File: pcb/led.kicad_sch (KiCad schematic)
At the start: 45 parts, among them Q10 2N7002KDW, Q6 2N7002KDW, Q7 2N7002KDW, Q8 2N7002KDW, Q9 2N7002KDW

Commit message: Fix JLC part association
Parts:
- D10, D11, D14, D15, D16, D7, D8, D9: JLC (none) -> C72043
- D12, D13: JLC (none) -> C72041
- Q10, Q6, Q7, Q8, Q9: JLC (none) -> C2912545
- R17, R19, R23, R24, R27, R33, R36, R40, R41, R44: JLC (none) -> C25744
- R18, R20, R25, R26, R30, R32, R34, R35, R37, R39, R42, R45: JLC (none) -> C11702
- R21, R22, R28, R29, R31, R38, R43, R46: JLC (none) -> C25890

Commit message: Update blue LEDs to stocked part
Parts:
- D12, D13: JLC C72041 -> C2288
- R32, R37: value 1k -> 2k2; JLC C11702 -> C25879
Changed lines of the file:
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@@
 			)
 		)
-		(property "Datasheet" "https://datasheet.lcsc.com/lcsc/1811101510_Everlight-Elec-19-217-BHC-ZL1M2RY-3T_C72041.pdf"
+		(property "Datasheet" "https://wmsc.lcsc.com/wmsc/upload/file/pdf/v2/lcsc/1810220913_Hubei-KENTO-Elec-KT-0603B_C2288.pdf"
 			(at 152.4 121.92 0)
 			(effects
@@
 			)
 		)
-		(property "JLC" "C72041"
+		(property "JLC" "C2288"
 			(at 152.4 121.92 0)
 			(effects
@@
 			)
 		)
-		(property "Value" "1k"
+		(property "Value" "2k2"
 			(at 154.94 132.7149 0)
 			(effects
@@
 			)
 		)
-		(property "JLC" "C11702"
+		(property "JLC" "C25879"
 			(at 152.4 131.445 0)
 			(effects
@@
 			)
 		)
-		(property "Value" "1k"
+		(property "Value" "2k2"
 			(at 186.69 88.2649 0)
 			(effects
@@
 			)
 		)
-		(property "JLC" "C11702"
+		(property "JLC" "C25879"
 			(at 184.15 86.995 0)
 			(effects
@@
 			)
 		)
-		(property "Datasheet" "https://datasheet.lcsc.com/lcsc/1811101510_Everlight-Elec-19-217-BHC-ZL1M2RY-3T_C72041.pdf"
+		(property "Datasheet" "https://wmsc.lcsc.com/wmsc/upload/file/pdf/v2/lcsc/1810220913_Hubei-KENTO-Elec-KT-0603B_C2288.pdf"
 			(at 184.15 77.47 0)
 			(effects
@@
 			)
 		)
-		(property "JLC" "C72041"
+		(property "JLC" "C2288"
 			(at 184.15 77.47 0)
 			(effects

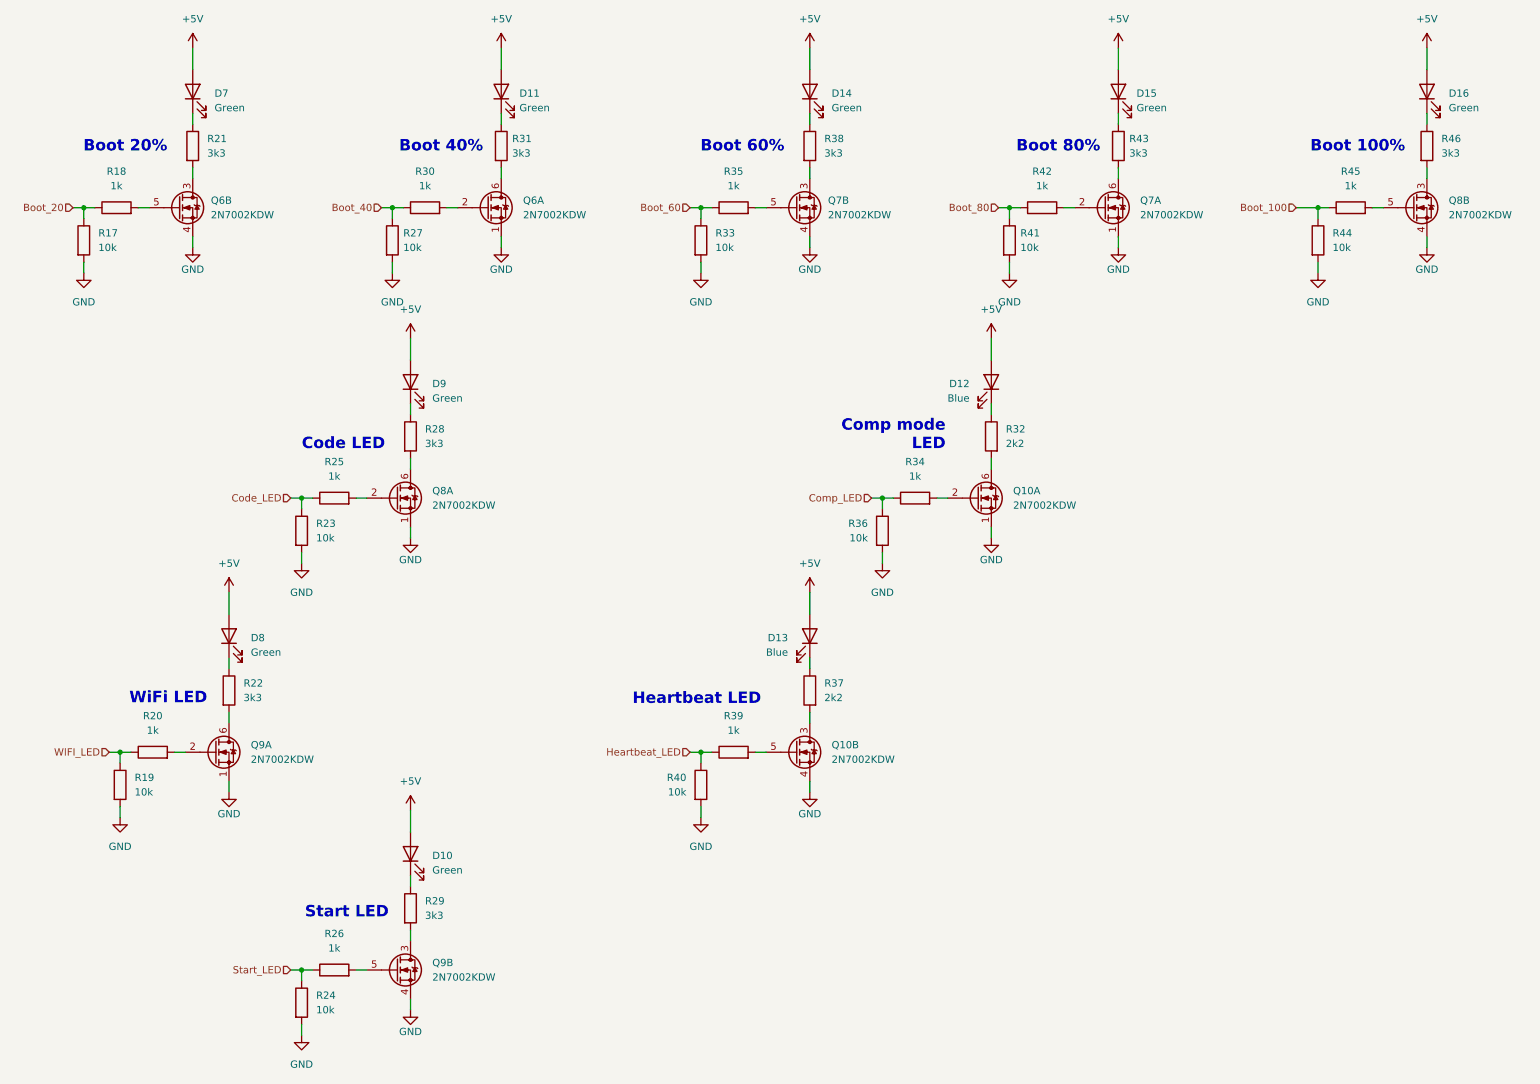
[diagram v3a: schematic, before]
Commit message: Fix ERC/DRC errors from Kicad 8
Mostly outdated library symbols and aligning the schmatic to the new grid
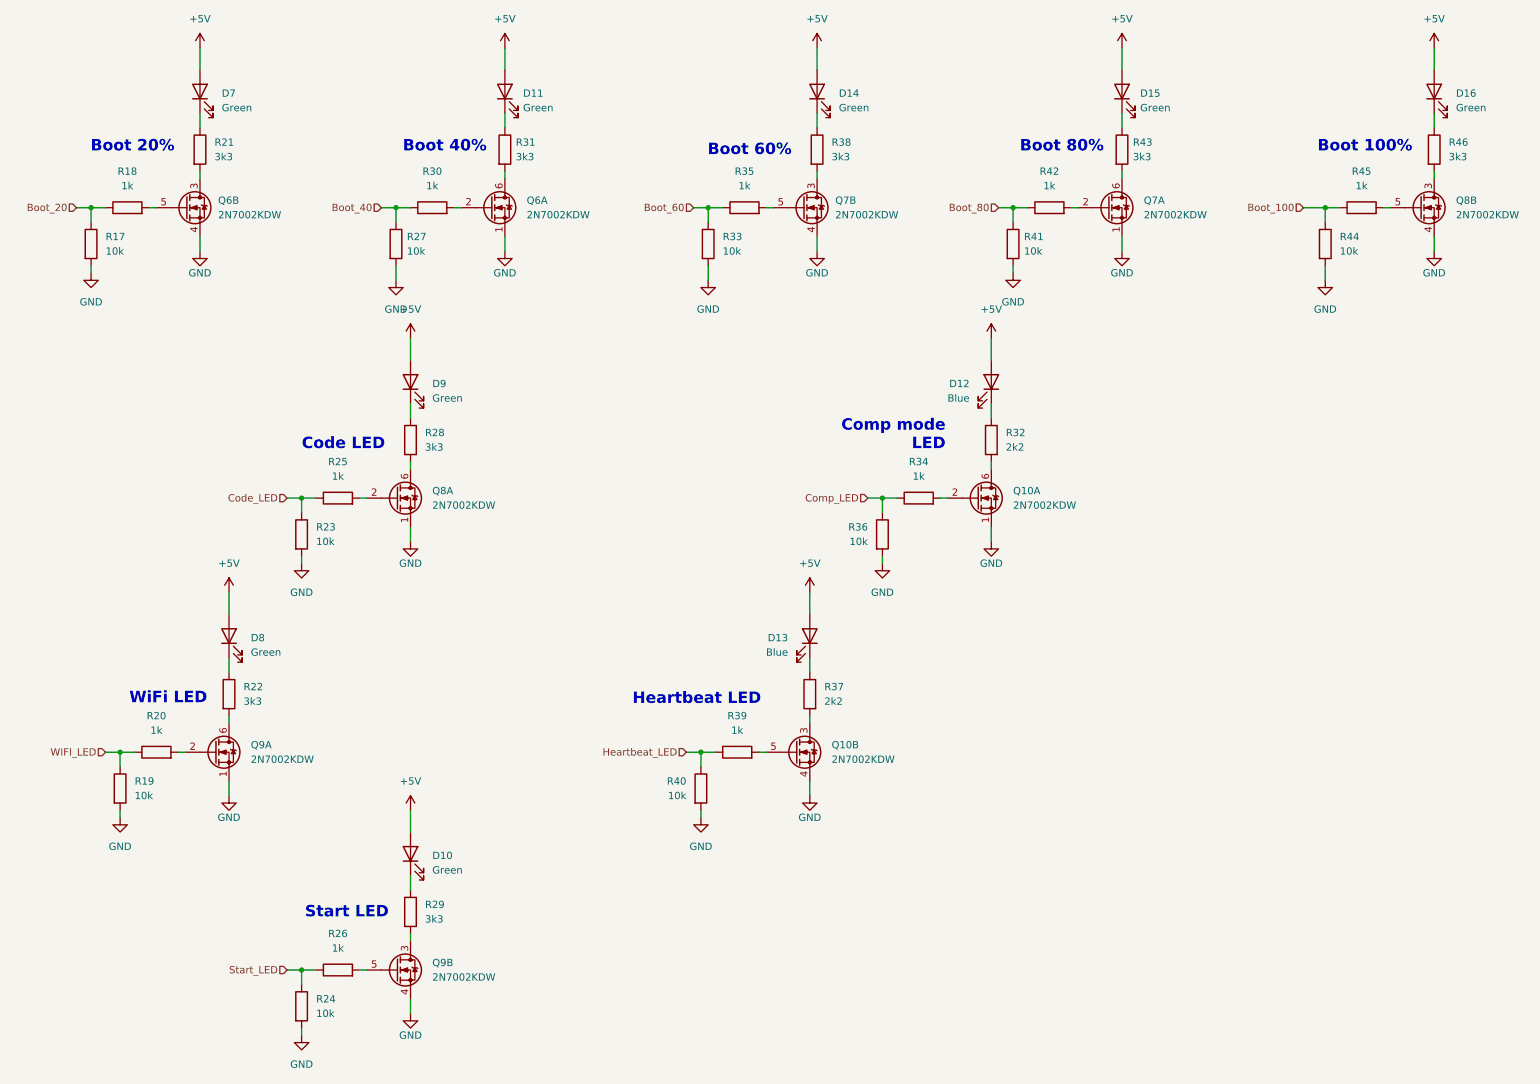
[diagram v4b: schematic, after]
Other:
- moved on the sheet: D11, D14, D15, D16, D7, Q6A, Q6B, Q7A, Q7B, Q8B, R17, R18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

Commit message: Switch 2N7002KDW to in stock version
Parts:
- Q10, Q6, Q7, Q8, Q9: JLC C2912545 -> C5174640
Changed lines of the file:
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@@
 			)
 		)
-		(property "JLC" "C2912545"
+		(property "JLC" "C5174640"
 			(at 96.52 46.99 0)
 			(effects
@@
 			)
 		)
-		(property "JLC" "C2912545"
+		(property "JLC" "C5174640"
 			(at 204.47 46.99 0)
 			(effects
@@
 			)
 		)
-		(property "JLC" "C2912545"
+		(property "JLC" "C5174640"
 			(at 259.08 46.99 0)
 			(effects
@@
 			)
 		)
-		(property "JLC" "C2912545"
+		(property "JLC" "C5174640"
 			(at 149.86 142.24 0)
 			(effects
@@
 			)
 		)
-		(property "JLC" "C2912545"
+		(property "JLC" "C5174640"
 			(at 181.61 97.79 0)
 			(effects
@@
 			)
 		)
-		(property "JLC" "C2912545"
+		(property "JLC" "C5174640"
 			(at 151.13 46.99 0)
 			(effects
@@
 			)
 		)
-		(property "JLC" "C2912545"
+		(property "JLC" "C5174640"
 			(at 80.01 180.34 0)
 			(effects
@@
 			)
 		)
-		(property "JLC" "C2912545"
+		(property "JLC" "C5174640"
 			(at 48.26 142.24 0)
 			(effects
@@
 			)
 		)
-		(property "JLC" "C2912545"
+		(property "JLC" "C5174640"
 			(at 43.18 46.99 0)
 			(effects
@@
 			)
 		)
-		(property "JLC" "C2912545"
+		(property "JLC" "C5174640"
 			(at 80.01 97.79 0)
 			(effects
